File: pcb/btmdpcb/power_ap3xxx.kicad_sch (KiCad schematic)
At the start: 8 parts, among them U7 AP3402

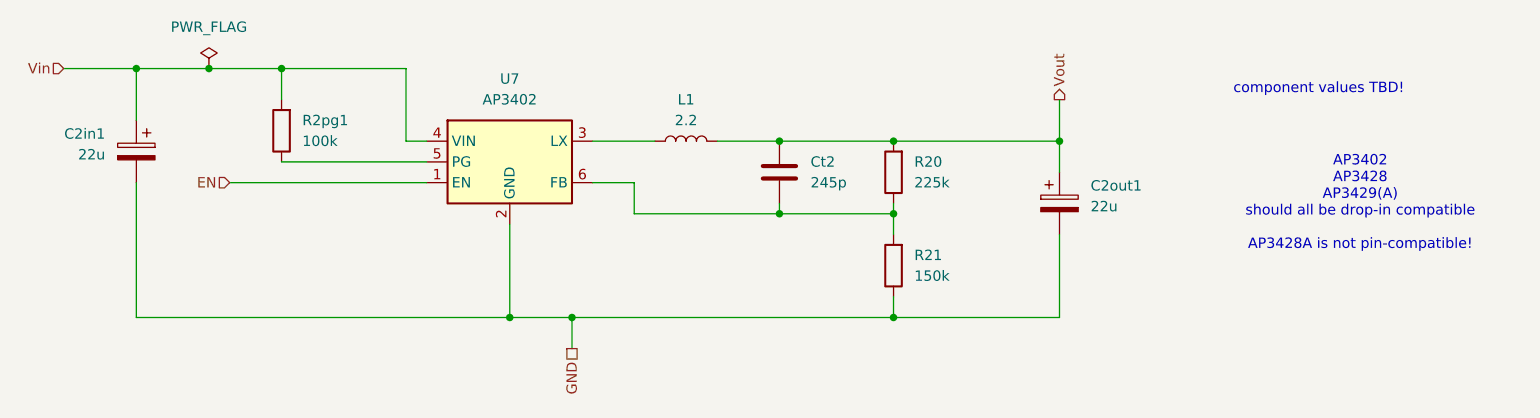
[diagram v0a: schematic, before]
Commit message: Clean up schematic, implement all logic functionality
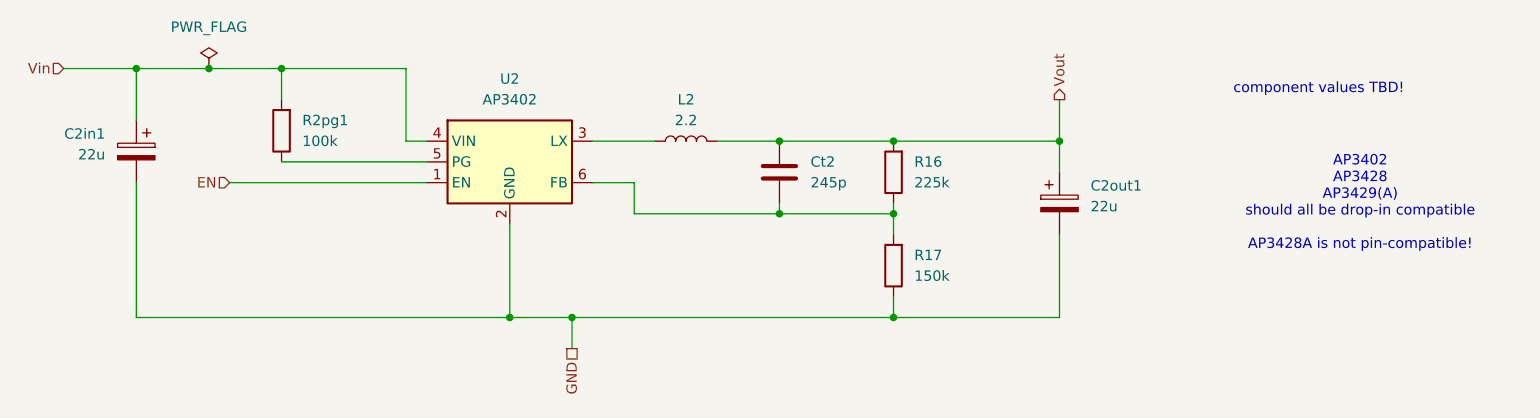
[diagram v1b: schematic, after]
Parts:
- renumbered L1 to L2, R20 to R16, R21 to R17, U7 to U2
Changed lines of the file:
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@@
 		(dnp no)
 		(fields_autoplaced yes)
-		(property "Reference" "R21"
+		(property "Reference" "R17"
 			(at 170.18 69.8499 0)
 			(effects
@@
 			(project "btmdpcb"
 				(path "/6e43e92f-e106-411c-86ee-217d084aee5b/a0c0f179-7687-45bf-a81b-4189df333c9d"
-					(reference "R21")
+					(reference "R17")
 					(unit 1)
 				)
@@
 		(on_board yes)
 		(dnp no)
-		(property "Reference" "L1"
+		(property "Reference" "L2"
 			(at 142.24 50.8 90)
 			(effects
@@
 			(project "btmdpcb"
 				(path "/6e43e92f-e106-411c-86ee-217d084aee5b/a0c0f179-7687-45bf-a81b-4189df333c9d"
-					(reference "L1")
+					(reference "L2")
 					(unit 1)
 				)
@@
 		(dnp no)
 		(fields_autoplaced yes)
-		(property "Reference" "R20"
+		(property "Reference" "R16"
 			(at 170.18 58.4199 0)
 			(effects
@@
 			(project "btmdpcb"
 				(path "/6e43e92f-e106-411c-86ee-217d084aee5b/a0c0f179-7687-45bf-a81b-4189df333c9d"
-					(reference "R20")
+					(reference "R16")
 					(unit 1)
 				)
@@
 		(dnp no)
 		(fields_autoplaced yes)
-		(property "Reference" "U7"
+		(property "Reference" "U2"
 			(at 120.65 48.26 0)
 			(effects
@@
 			(project "btmdpcb"
 				(path "/6e43e92f-e106-411c-86ee-217d084aee5b/a0c0f179-7687-45bf-a81b-4189df333c9d"
-					(reference "U7")
-					(unit 1)
-				)
+					(reference "U2")
+					(unit 1)
+				)
